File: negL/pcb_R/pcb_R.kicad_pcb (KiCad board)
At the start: 2 copper layers, 162.7 x 113.5 mm, 116 parts, among them J1 MJ-4PP-9, J2 FH-1x4SG/RH, J3 XA-3-2-7P, Q1 AO3401A, SW1 TVBP06-B043CB-B, SW2 EVQWGD001, U1 nice_nano, U2 74HC595, U3 AE-XCL103-3V3

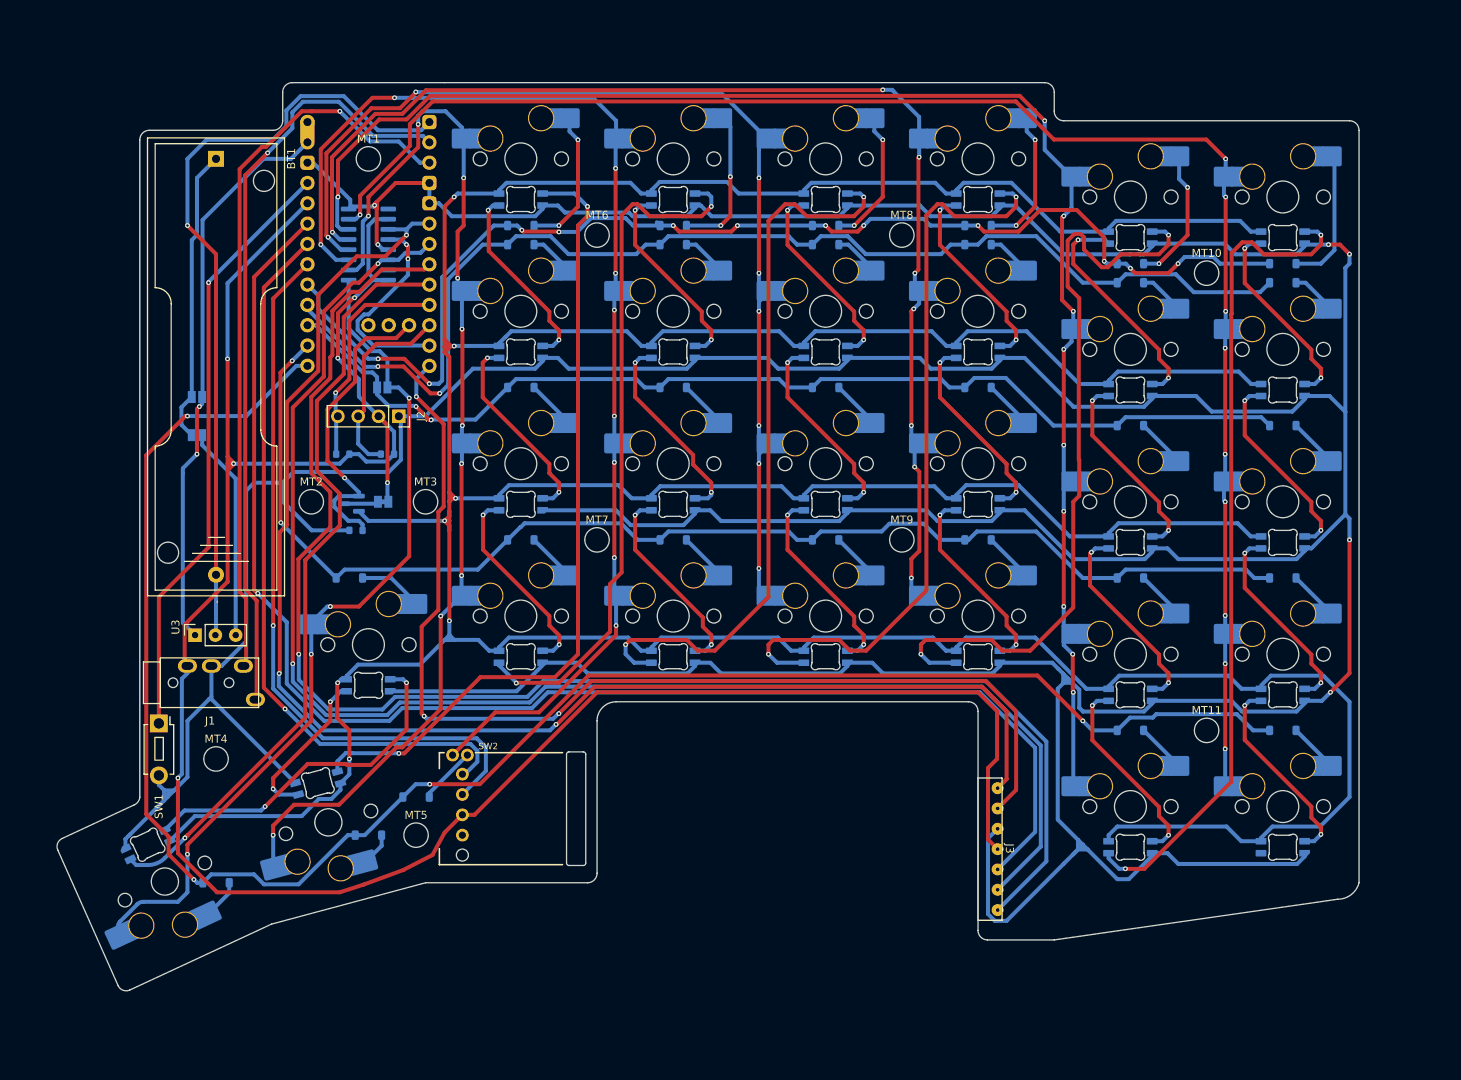
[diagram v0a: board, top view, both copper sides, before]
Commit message: Add switches
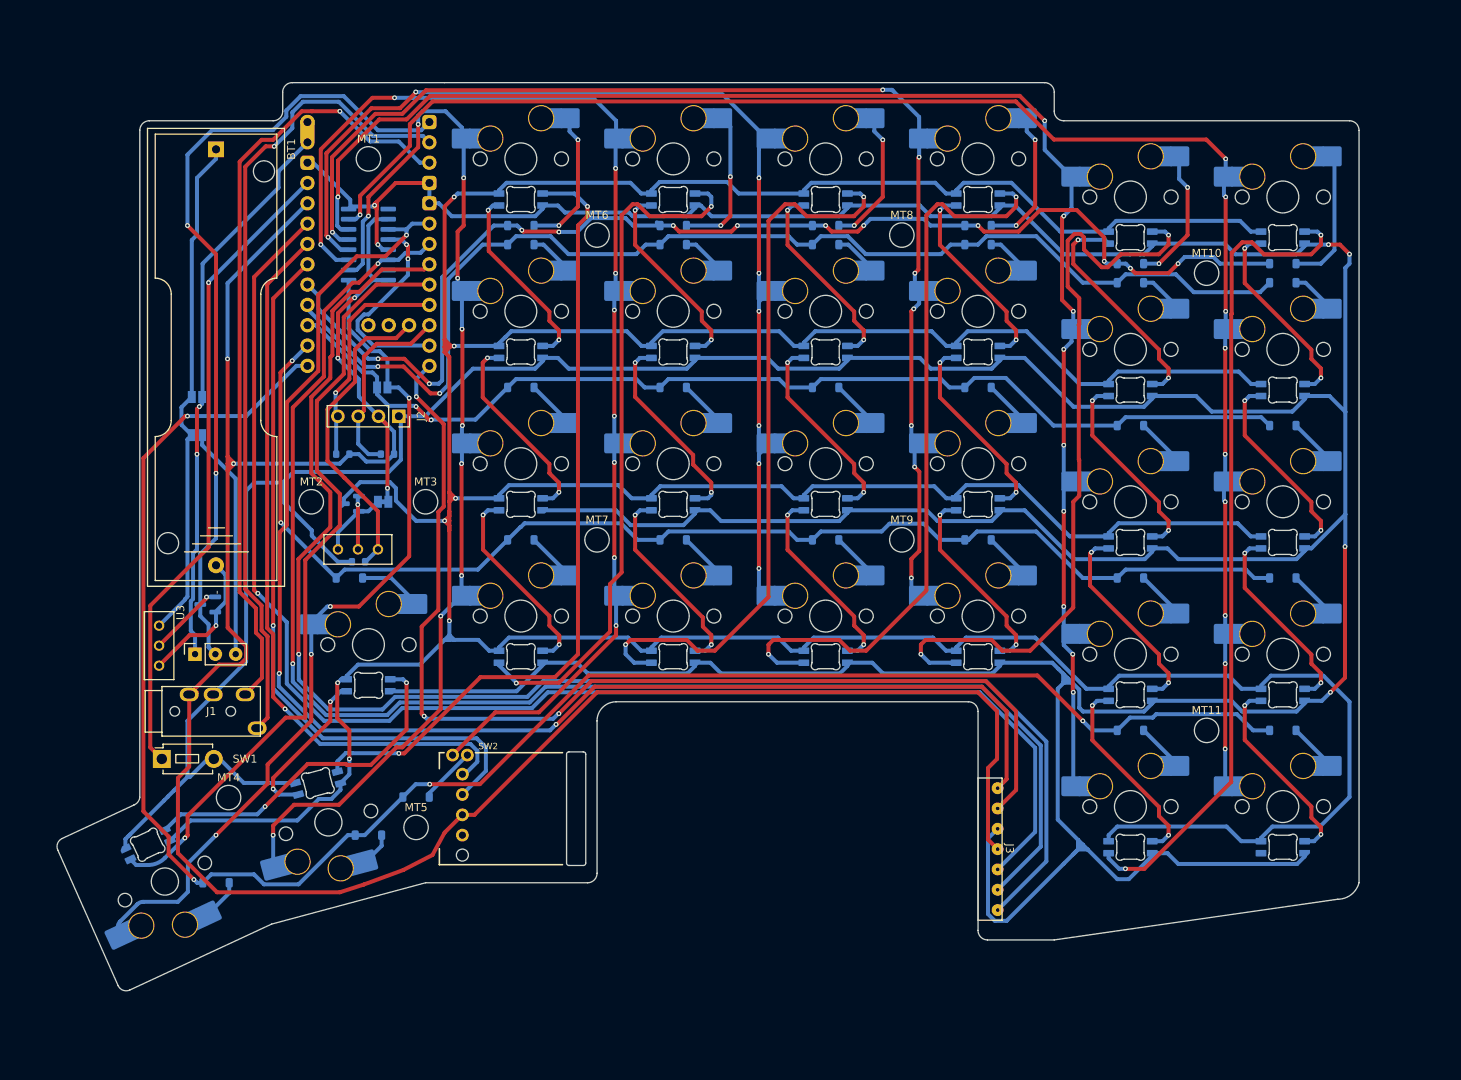
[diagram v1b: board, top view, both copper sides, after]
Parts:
- added Q2: AO3400A, Package_TO_SOT_SMD:SOT-23, B.Cu at (78.7, 106.9)
- added SW3: SS-12D00G3, neg_footprints:SS-12D00G3, F.Cu at (72.7, 112.0)
- added SW4: SS-12D00G3, neg_footprints:SS-12D00G3, F.Cu at (97.5, 100.0)
- R3: value 0603WAF2004T5E -> 0603WAF1004T5E
- moved MT4 5.08 mm to (81.3, 131.0)
- moved SW1 4.46 mm to (73.0, 126.2), turned to 0 degrees
- moved R3 3.94 mm to (97.6, 101.6)
- moved J1 3.58 mm to (79.2, 120.3)
- moved U3 2.38 mm to (79.7, 112.1)
- moved BT1 1.19 mm to (79.8, 50.0)
- moved MT5 0.97 mm to (104.8, 134.8)
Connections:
- BT1 pad 2: BAT- -> Net-(BT1--)
- Q1 pad 1: LED_POWER -> Net-(Q1-G)
- Q1 pad 2: Net-(LED1-VDD) -> Net-(JP2-B)
- Q1 pad 3: Net-(JP2-B) -> Net-(LED1-VDD)
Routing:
- net Net-(BT1-+): track 36.2 -> 63.6 mm
- net Net-(BT1--): track 0.00 -> 17.8 mm, vias 0 -> 1
- net Net-(Q2-G): track 0.00 -> 9.64 mm, vias 0 -> 1
- net Net-(Q1-G): track 0.00 -> 6.73 mm, vias 0 -> 1
- net Net-(LED1-VDD): track 635.8 -> 642.1 mm
- net DATA_RX: track 91.9 -> 97.6 mm
- net RESET: track 75.2 -> 80.7 mm
- net DATA_TX: track 96.3 -> 101.5 mm
- net Net-(JP2-B): track 4.36 -> 8.72 mm
- net VCC: track 297.4 -> 301.6 mm, vias 6 -> 5
- net BAT-: track 97.9 -> 101.4 mm, vias 1 -> 2
- net GND: track 781.8 -> 778.8 mm
- net Net-(JP4-A): track 26.7 -> 29.1 mm
- net LED: track 96.9 -> 98.4 mm
- net LED_POWER: track 38.7 -> 39.8 mm, vias 1 -> 0
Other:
- outline, holes or cut-outs redrawn

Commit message: update
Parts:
- added JP10: ~, Jumper:SolderJumper-2_P1.3mm_Open_Pad1.0x1.5mm, B.Cu at (84.5, 60.7)
- added JP7: ~, Jumper:SolderJumper-2_P1.3mm_Open_Pad1.0x1.5mm, B.Cu at (79.8, 56.0)
- added JP8: ~, Jumper:SolderJumper-2_P1.3mm_Open_Pad1.0x1.5mm, B.Cu at (84.5, 56.0)
- added JP9: ~, Jumper:SolderJumper-2_P1.3mm_Open_Pad1.0x1.5mm, B.Cu at (79.8, 60.7)
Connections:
- J1 pad R1: DATA_RX -> Net-(JP7-A)
- J1 pad T: DATA_TX -> Net-(JP10-A)
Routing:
- net Net-(JP10-A): track 0.00 -> 68.5 mm, vias 0 -> 1
- net Net-(JP7-A): track 0.00 -> 65.7 mm, vias 0 -> 1
- net DATA_TX: track 101.5 -> 39.2 mm, vias 1 -> 0
- net DATA_RX: track 97.6 -> 40.9 mm, vias 1 -> 4
- net DISP_SCL: track 24.4 -> 23.5 mm
- net DISP_SDA: track 28.4 -> 29.1 mm

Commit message: update
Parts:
- moved JP1 19.3 mm to (82.2, 85.7), turned to 0 degrees
- moved D26 2.38 mm to (82.2, 141.7)
- renumbered JP7 to JP5, JP8 to JP6, JP9 to JP7, JP10 to JP8
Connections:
- JP1 pad 2: ROW2 -> ROW3
- MX1 pad 1: COL1 -> COL2
- MX10 pad 1: COL4 -> COL5
- MX11 pad 1: COL5 -> COL6
- MX12 pad 1: COL6 -> COL7
- MX13 pad 1: COL1 -> COL2
- MX14 pad 1: COL2 -> COL3
- MX15 pad 1: COL3 -> COL4
- MX16 pad 1: COL4 -> COL5
- MX17 pad 1: COL5 -> COL6
- MX18 pad 1: COL6 -> COL7
- MX19 pad 1: COL0 -> COL1
- MX2 pad 1: COL2 -> COL3
- MX20 pad 1: COL1 -> COL2
- MX21 pad 1: COL2 -> COL3
- MX22 pad 1: COL3 -> COL4
- MX23 pad 1: COL4 -> COL5
- MX24 pad 1: COL5 -> COL6
- MX25 pad 1: COL6 -> COL7
- MX26 pad 1: COL5 -> COL6
- MX27 pad 1: COL6 -> COL7
- MX3 pad 1: COL3 -> COL4
- MX4 pad 1: COL4 -> COL5
- MX5 pad 1: COL5 -> COL6
- MX6 pad 1: COL6 -> COL7
- MX7 pad 1: COL1 -> COL2
- MX8 pad 1: COL2 -> COL3
- MX9 pad 1: COL3 -> COL4
- U2 pad 1: COL0 -> COL1
- U2 pad 15: unconnected-(U2-QA-Pad15) -> COL0
- U2 pad 2: COL1 -> COL2
- U2 pad 3: COL2 -> COL3
- U2 pad 4: COL3 -> COL4
- U2 pad 5: COL4 -> COL5
- U2 pad 6: COL5 -> COL6
- U2 pad 7: COL6 -> COL7
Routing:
- net COL7: track 0.00 -> 201.1 mm, vias 0 -> 10
- net COL1: track 136.9 -> 88.7 mm, vias 10 -> 4
- net COL5: track 191.1 -> 153.9 mm, vias 10 -> 8
- net COL2: track 148.2 -> 114.7 mm
- net COL4: track 153.9 -> 134.0 mm
- net COL3: track 134.0 -> 116.8 mm
- net COL6: track 201.1 -> 191.1 mm
- net ROW3: track 160.0 -> 167.5 mm, vias 2 -> 3
- net COL0: track 106.9 -> 111.5 mm
- net BAT+: track 70.2 -> 73.3 mm
- net Net-(LED3-DOUT): track 99.7 -> 101.7 mm
- net Net-(D26-A): track 4.94 -> 6.57 mm
- net LED: track 98.4 -> 97.0 mm
- net COL_NCS: track 26.0 -> 26.9 mm
- net ENC_B: track 91.5 -> 92.4 mm
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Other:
- board text added: "NOTE: BLE Micro ProではBATは1ピンのみで 下のピンが5V出力ピンとなっているため、 上のピンのみをBAT+として扱うこと"

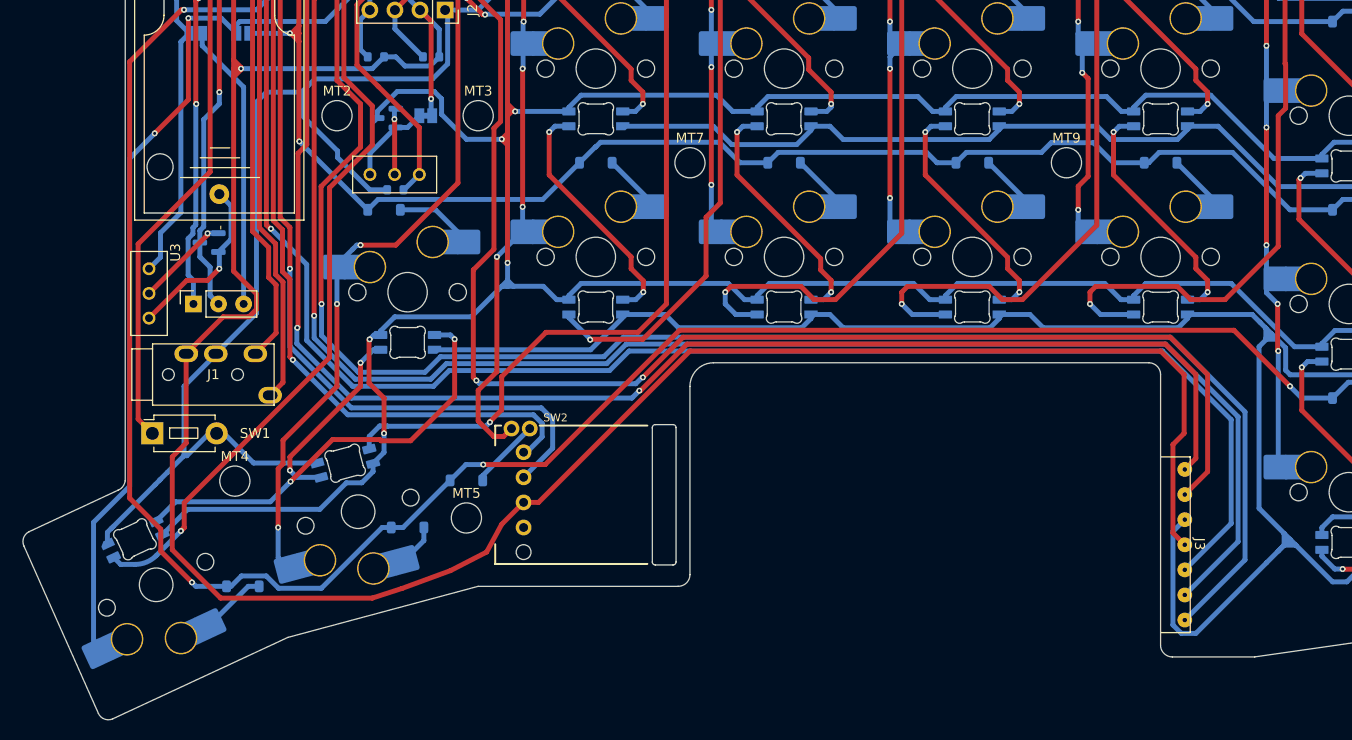
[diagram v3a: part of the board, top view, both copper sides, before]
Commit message: change encoder position
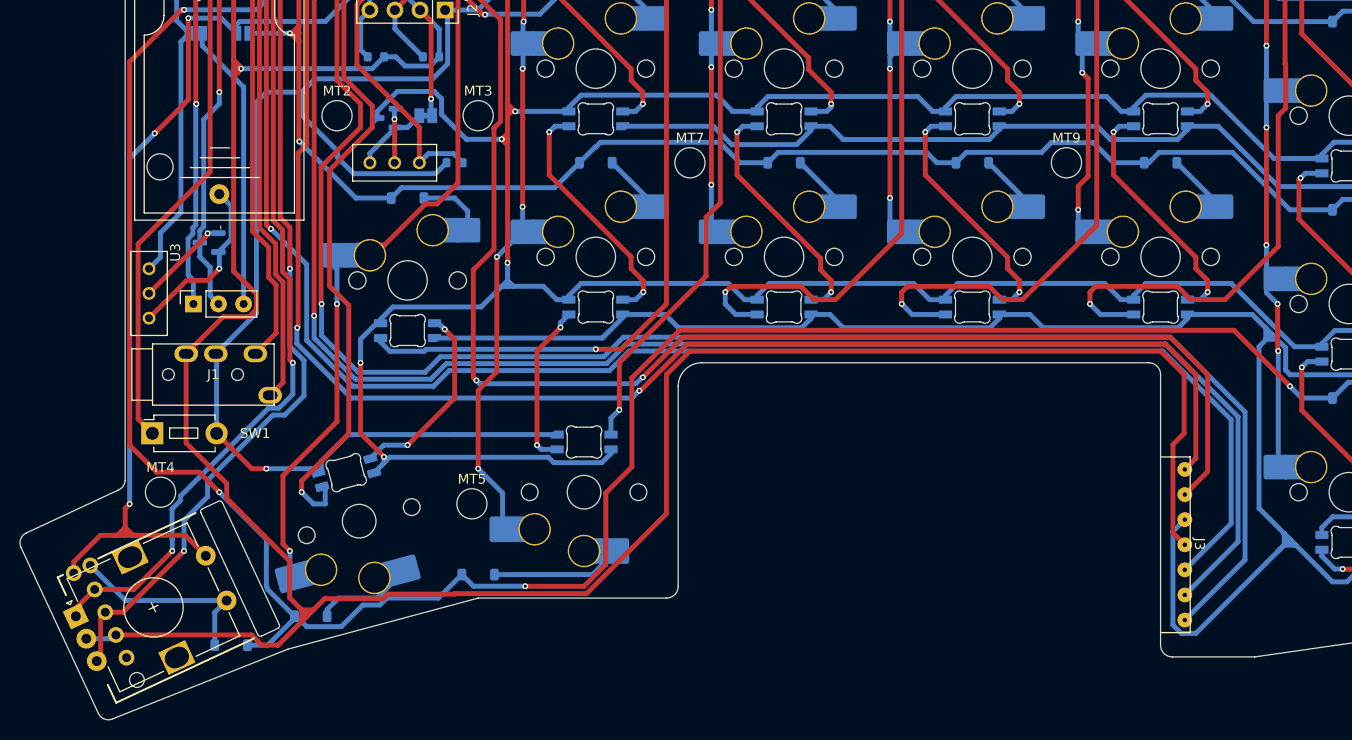
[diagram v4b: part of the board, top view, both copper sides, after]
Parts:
- SW2: footprint neg_footprints:RollerEncoder_Panasonic_EVQWGD001 -> neg_footprints:EVQWGD001_EC12
- moved SW2 43.8 mm to (73.9, 143.1), turned to 25 degrees
- moved D30 29.1 mm to (81.0, 147.6), turned to 180 degrees
- moved LED3 24.3 mm to (116.7, 127.1), turned to 0 degrees
- moved CH2 22.9 mm to (116.7, 132.2), turned to 180 degrees
- moved LED1 22.4 mm to (92.6, 130.2), turned to 15 degrees
- moved CH1 21.5 mm to (93.9, 135.1), turned to -165 degrees
- moved D27 8.59 mm to (106.0, 140.5)
- moved MT4 7.61 mm to (73.8, 132.2)
- moved D26 7.52 mm to (89.0, 144.7)
- moved R3 6.60 mm to (103.6, 98.8)
- moved D19 2.66 mm to (98.8, 102.4)
- moved MT5 1.54 mm to (105.3, 133.3)
- moved LED2 1.19 mm to (98.8, 115.8)
- moved MX19 1.19 mm to (98.8, 110.7)
- moved SW4 1.19 mm to (97.5, 98.8)
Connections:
- CH1 pad 1: COL0 -> COL1
- CH2 pad 1: COL1 -> COL2
- LED3 pad 3: Net-(LED2-DOUT) -> Net-(LED3-DIN)
- LED4 pad 3: Net-(LED3-DOUT) -> Net-(LED2-DOUT)
- LED7 pad 2: Net-(LED7-DOUT) -> Net-(LED3-DIN)
- LED8 pad 3: Net-(LED7-DOUT) -> Net-(LED3-DOUT)
- SW2 pad S1: COL2 -> COL0
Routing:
- net Net-(LED7-DOUT): track 86.8 -> 0.00 mm, vias 2 -> 0
- net Net-(LED2-DOUT): track 19.9 -> 94.4 mm
- net VCC: track 301.9 -> 333.5 mm
- net Net-(LED1-DOUT): track 43.6 -> 19.7 mm
- net ROW4: track 231.5 -> 248.9 mm
- net Net-(LED3-DIN): track 0.00 -> 16.8 mm, vias 0 -> 2
- net Net-(D30-A): track 7.22 -> 20.3 mm
- net Net-(LED3-DOUT): track 101.7 -> 89.0 mm
- net GND: track 778.8 -> 790.3 mm, vias 6 -> 7
- net LED: track 97.0 -> 85.5 mm
- net Net-(D27-A): track 4.13 -> 13.3 mm
- net COL2: track 114.7 -> 122.3 mm, vias 9 -> 10
- net ENC_A: track 92.0 -> 98.2 mm, vias 1 -> 2
- net ENC_B: track 92.4 -> 98.5 mm, vias 1 -> 2
- net COL0: track 111.5 -> 116.6 mm, vias 4 -> 5
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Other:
- board size 162.7 x 113.5 mm -> 163 x 113.5 mm

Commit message: update
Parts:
- U1: footprint PCM_marbastlib-xp-promicroish:nice_nano_AH_USBup -> neg_footprints:promicro_nrf
- moved U1 3.00 mm to (97.7, 60.3)
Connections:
- U1 pad 13: BAT+ -> unconnected-(U1-BAT+-Pad13)
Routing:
- net LED: track 85.5 -> 88.9 mm
- net Net-(D26-A): track 10.3 -> 11.4 mm
- net COL1: track 89.2 -> 88.6 mm
- net COL7: track 201.1 -> 201.7 mm
- net GND: vias 7 -> 23
- added copper zone on B.Cu, net GND
- added copper zone on F.Cu, net GND
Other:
- board text removed: "NOTE: BLE Micro ProではBATは1ピンのみで 下のピンが5V出力ピンとなっているため、 上のピンのみをBAT+として扱うこと"

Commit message: update
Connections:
- U1 pad 13: unconnected-(U1-BAT+-Pad13) -> BAT+
- U1 pad 29: BAT+ -> unconnected-(U1-BAT+-Pad29)
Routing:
- net BAT+: track 73.4 -> 70.4 mm

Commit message: update
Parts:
- removed Q2: AO3400A, Package_TO_SOT_SMD:SOT-23
- added BT2: JST_PH_S2B, Connector_JST:JST_PH_S2B-PH-K_1x02_P2.00mm_Horizontal, F.Cu at (84.3, 54.8)
- added C1: CL10A106KP8NNNC, Capacitor_SMD:C_0603_1608Metric, B.Cu at (76.2, 74.9)
- added C2: CL10A106KP8NNNC, Capacitor_SMD:C_0603_1608Metric, B.Cu at (76.1, 81.7)
- added C3: CL10A106KP8NNNC, Capacitor_SMD:C_0603_1608Metric, B.Cu at (76.4, 55.7)
- added C4: CL10A226MQ8NRNC, Capacitor_SMD:C_0603_1608Metric, B.Cu at (72.8, 62.4)
- added D31: SS12, Diode_SMD:D_SMA, B.Cu at (82.8, 48.5)
- added IC1: SN74LVC4245A, neg_footprints:TSSOP-24, B.Cu at (77.4, 100.0)
- added JP10: LED switch input, Jumper:SolderJumper-2_P1.3mm_Open_Pad1.0x1.5mm, F.Cu at (98.8, 94.1)
- added JP11: LED_VCC Direct, Jumper:SolderJumper-2_P1.3mm_Open_Pad1.0x1.5mm, B.Cu at (76.2, 85.7)
- added JP12: ~, Jumper:SolderJumper-2_P1.3mm_Open_Pad1.0x1.5mm, B.Cu at (81.0, 91.0)
- added JP13: ~, Jumper:SolderJumper-2_P1.3mm_Open_Pad1.0x1.5mm, B.Cu at (81.0, 93.6)
- added JP9: LED_VCC 5V, Jumper:SolderJumper-2_P1.3mm_Open_Pad1.0x1.5mm, B.Cu at (76.2, 71.4)
- added L1: SDFL1608Q4R7KTF, Inductor_SMD:L_0603_1608Metric, B.Cu at (76.2, 73.4)
- added L2: SDFL1608Q4R7KTF, Inductor_SMD:L_0603_1608Metric, B.Cu at (76.4, 54.1)
- added R4: 0603WAF4992T5E, Resistor_SMD:R_0603_1608Metric, B.Cu at (73.3, 78.3)
- added R5: 0603WAF5601T5E, Resistor_SMD:R_0603_1608Metric, B.Cu at (76.1, 80.1)
- added R6: 0603WAF1003T5E, Resistor_SMD:R_0603_1608Metric, B.Cu at (73.1, 58.4)
- added R7: 0603WAF1802T5E, Resistor_SMD:R_0603_1608Metric, B.Cu at (76.0, 60.9)
- added U4: TLV61070ADBV, Package_TO_SOT_SMD:SOT-23-6, B.Cu at (76.5, 58.3)
- JP1: value Hand Jumper -> ~
- JP2: value LED Jumper -> ~; footprint Jumper:SolderJumper-2_P1.3mm_Bridged_Pad1.0x1.5mm -> Jumper:SolderJumper-2_P1.3mm_Open_Pad1.0x1.5mm
- JP4: value ~ -> Hand Jumper
- Q1: value AO3401A -> AO3400A
- U3: value AE-XCL103-3V3 -> TLV61070ADBV; footprint neg_footprints:AE-XCL103-3V3_Vertical -> Package_TO_SOT_SMD:SOT-23-6; moved to B.Cu
- moved SW3 60.9 mm to (75.0, 51.2), turned to 180 degrees
- moved Q1 46.3 mm to (72.4, 54.9)
- moved JP2 38.5 mm to (76.2, 64.3)
- moved U3 34.9 mm to (76.1, 77.4), turned to 180 degrees
- moved MT11 20.3 mm to (210.7, 141.7)
- moved JP1 18.8 mm to (76.2, 67.9), turned to 180 degrees
- moved JP6 12.0 mm to (83.3, 67.9)
- moved JP5 11.9 mm to (79.8, 67.9)
- moved BT1 10.9 mm to (79.8, 60.9)
- moved JP8 10.8 mm to (83.3, 71.4)
- moved JP7 10.7 mm to (79.8, 71.4)
- moved JP3 10.6 mm to (72.6, 71.4)
- moved JP4 3.57 mm to (81.0, 85.7), turned to 0 degrees
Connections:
- JP1 pad 1: COL0 -> BAT+
- JP1 pad 2: ROW3 -> Net-(BT1-+)
- JP2 pad 1: VCC -> Net-(JP2-A)
- JP2 pad 2: Net-(JP2-B) -> Net-(BT1-+)
- JP3 pad 1: Net-(BT1-+) -> Net-(D31-K)
- JP4 pad 1: Net-(JP4-A) -> COL0
- JP4 pad 2: Net-(BT1-+) -> ROW3
- LED1 pad 1: Net-(LED1-VDD) -> LED_VCC
- LED1 pad 3: LED -> Net-(IC1-B1)
- LED10 pad 1: Net-(LED1-VDD) -> LED_VCC
- LED11 pad 1: Net-(LED1-VDD) -> LED_VCC
- LED12 pad 1: Net-(LED1-VDD) -> LED_VCC
- LED13 pad 1: Net-(LED1-VDD) -> LED_VCC
- LED14 pad 1: Net-(LED1-VDD) -> LED_VCC
- LED15 pad 1: Net-(LED1-VDD) -> LED_VCC
- LED16 pad 1: Net-(LED1-VDD) -> LED_VCC
- LED17 pad 1: Net-(LED1-VDD) -> LED_VCC
- LED18 pad 1: Net-(LED1-VDD) -> LED_VCC
- LED19 pad 1: Net-(LED1-VDD) -> LED_VCC
- LED2 pad 1: Net-(LED1-VDD) -> LED_VCC
- LED20 pad 1: Net-(LED1-VDD) -> LED_VCC
- LED21 pad 1: Net-(LED1-VDD) -> LED_VCC
- LED22 pad 1: Net-(LED1-VDD) -> LED_VCC
- LED23 pad 1: Net-(LED1-VDD) -> LED_VCC
- LED24 pad 1: Net-(LED1-VDD) -> LED_VCC
- LED25 pad 1: Net-(LED1-VDD) -> LED_VCC
- LED26 pad 1: Net-(LED1-VDD) -> LED_VCC
- LED27 pad 1: Net-(LED1-VDD) -> LED_VCC
- LED28 pad 1: Net-(LED1-VDD) -> LED_VCC
- LED29 pad 1: Net-(LED1-VDD) -> LED_VCC
- LED3 pad 1: Net-(LED1-VDD) -> LED_VCC
- LED4 pad 1: Net-(LED1-VDD) -> LED_VCC
- LED5 pad 1: Net-(LED1-VDD) -> LED_VCC
- LED6 pad 1: Net-(LED1-VDD) -> LED_VCC
- LED7 pad 1: Net-(LED1-VDD) -> LED_VCC
- LED8 pad 1: Net-(LED1-VDD) -> LED_VCC
- LED9 pad 1: Net-(LED1-VDD) -> LED_VCC
- Q1 pad 2: Net-(JP2-B) -> Net-(BT1--)
- Q1 pad 3: Net-(LED1-VDD) -> BAT-
- R3 pad 1: LED_POWER -> Net-(JP10-A)
- SW3 pad 1: Net-(BT1-+) -> BAT+
- SW3 pad 2: Net-(Q2-G) -> Net-(Q1-G)
- SW4 pad 1: Net-(JP2-B) -> VCC
- SW4 pad 2: Net-(Q1-G) -> Net-(JP11-A)
- SW4 pad 3: LED_POWER -> Net-(JP10-A)
- U1 pad 17: BALL_MOTION -> LED_POWER
- U1 pad 25: LED_POWER -> BALL_MOTION
- U3 pad 1: BAT+ -> Net-(U3-SW)
- U3 pad 2: BAT- -> GND
- U3 pad 3: Net-(JP4-A) -> Net-(JP11-A)
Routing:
- net LED_VCC: track 0.00 -> 701.2 mm, vias 0 -> 7
- net Net-(LED1-VDD): track 645.1 -> 0.00 mm, vias 7 -> 0
- net Net-(BT1--): track 17.8 -> 95.8 mm, vias 1 -> 2
- net Net-(IC1-B1): track 0.00 -> 56.3 mm, vias 0 -> 2
- net BAT-: track 101.4 -> 45.6 mm, vias 2 -> 0
- net Net-(BT1-+): track 63.6 -> 12.9 mm
- net Net-(JP11-A): track 0.00 -> 47.8 mm, vias 0 -> 4
- net GND: track 790.3 -> 837.3 mm, vias 23 -> 44
- net LED: track 88.9 -> 47.2 mm
- net Net-(D31-K): track 0.00 -> 29.9 mm, vias 0 -> 2
- net Net-(JP4-A): track 29.1 -> 0.00 mm
- net BAT+: track 70.4 -> 45.1 mm, vias 2 -> 0
- net VCC: track 333.7 -> 354.5 mm, vias 5 -> 6
- net Net-(JP2-A): track 0.00 -> 19.9 mm
- net BALL_MOTION: track 179.0 -> 166.0 mm
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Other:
- board text added: "v0.1"
- board text removed: "test1"
